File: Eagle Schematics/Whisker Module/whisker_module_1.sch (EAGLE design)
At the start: 135 parts, among them IC1 74LS14N, IC2 74LS14N, IC3 74LS14N, IC4 74LS14N, IC5 74LS14N, IC6 74LS14N, IC7 74LS14N, M1 CD74HCT151E, M2 CD74HCT151E, M3 CD74HCT151E, M4 CD74HCT151E, M5 CD74HCT151E, X1 22-23-2021, X10 22-23-2021, X11 22-23-2021, X12 22-23-2021, X13 22-23-2021, X14 22-23-2021, X15 22-23-2021, X16 22-23-2021, X17 22-23-2021, X18 22-23-2021, X19 22-23-2021, X2 22-23-2021, X20 22-23-2021, X21 22-23-2021, X22 22-23-2021, X23 22-23-2021, X24 22-23-2021, X25 22-23-2021, X26 22-23-2021, X27 22-23-2021, X28 22-23-2021, X29 22-23-2021, X3 22-23-2021, X30 22-23-2021, X31 22-23-2021, X32 22-23-2021, X33 22-23-2021, X34 22-23-2021, X35 22-23-2021, X36 22-23-2021, X37 22-23-2021, X38 22-23-2021, X39 22-23-2021, X4 22-23-2021, X40 22-23-2021, X5 22-23-2021, X6 22-23-2021, X7 22-23-2021, X8 22-23-2021, X9 22-23-2021

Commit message: Finished V1.0 whisker module
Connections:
- removed net N$2: X1-1.S, X10-1.S, X11-1.S, X12-1.S, X13-1.S, X14-1.S, X15-1.S, X16-1.S, X17-1.S, X18-1.S, X19-1.S, X2-1.S, X20-1.S, X21-1.S, X22-1.S, X23-1.S, X24-1.S, X25-1.S, X26-1.S, X27-1.S, X28-1.S, X29-1.S, X3-1.S, X30-1.S, X31-1.S, X32-1.S, X33-1.S, X34-1.S, X35-1.S, X36-1.S, X37-1.S, X38-1.S, X39-1.S, X4-1.S, X40-1.S, X5-1.S, X6-1.S, X7-1.S, X8-1.S, X9-1.S
- net GND: now also X1-1.S, X10-1.S, X11-1.S, X12-1.S, X13-1.S, X14-1.S, X15-1.S, X16-1.S, X17-1.S, X18-1.S, X19-1.S, X2-1.S, X20-1.S, X21-1.S, X22-1.S, X23-1.S, X24-1.S, X25-1.S, X26-1.S, X27-1.S, X28-1.S, X29-1.S, X3-1.S, X30-1.S, X31-1.S, X32-1.S, X33-1.S, X34-1.S, X35-1.S, X36-1.S, X37-1.S, X38-1.S, X39-1.S, X4-1.S, X40-1.S, X5-1.S, X6-1.S, X7-1.S, X8-1.S, X9-1.S

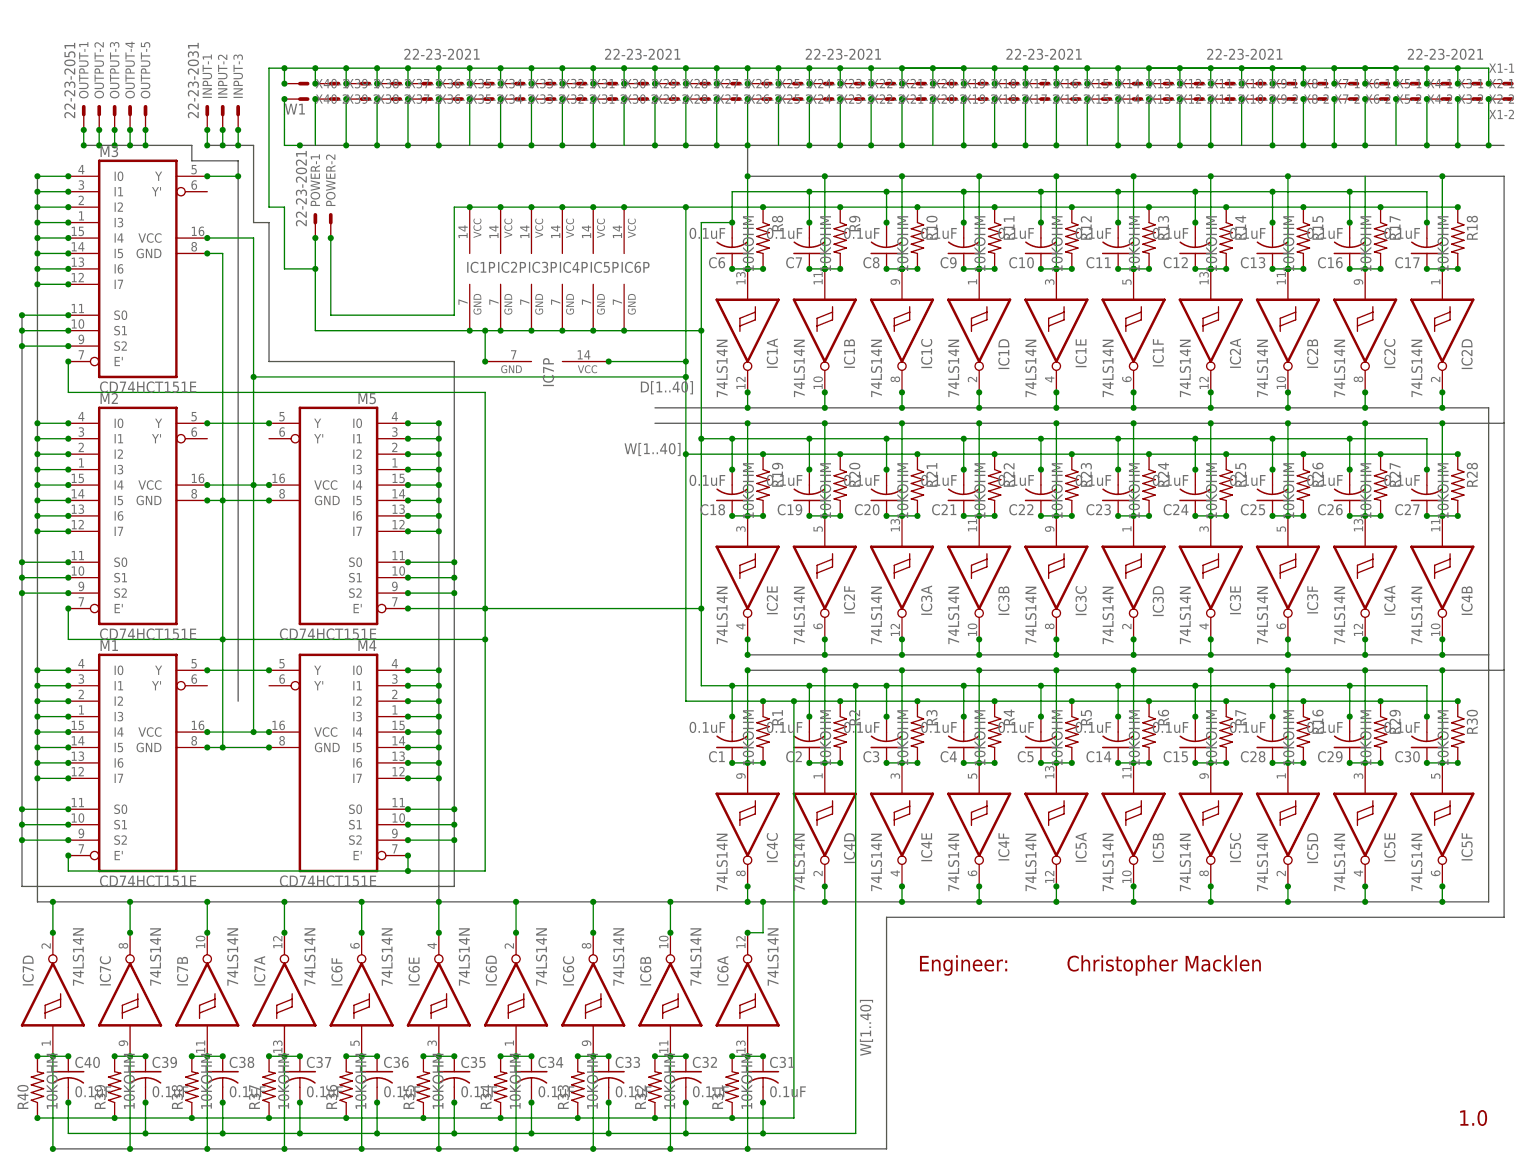
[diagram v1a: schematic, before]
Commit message: Finished both whisker modules
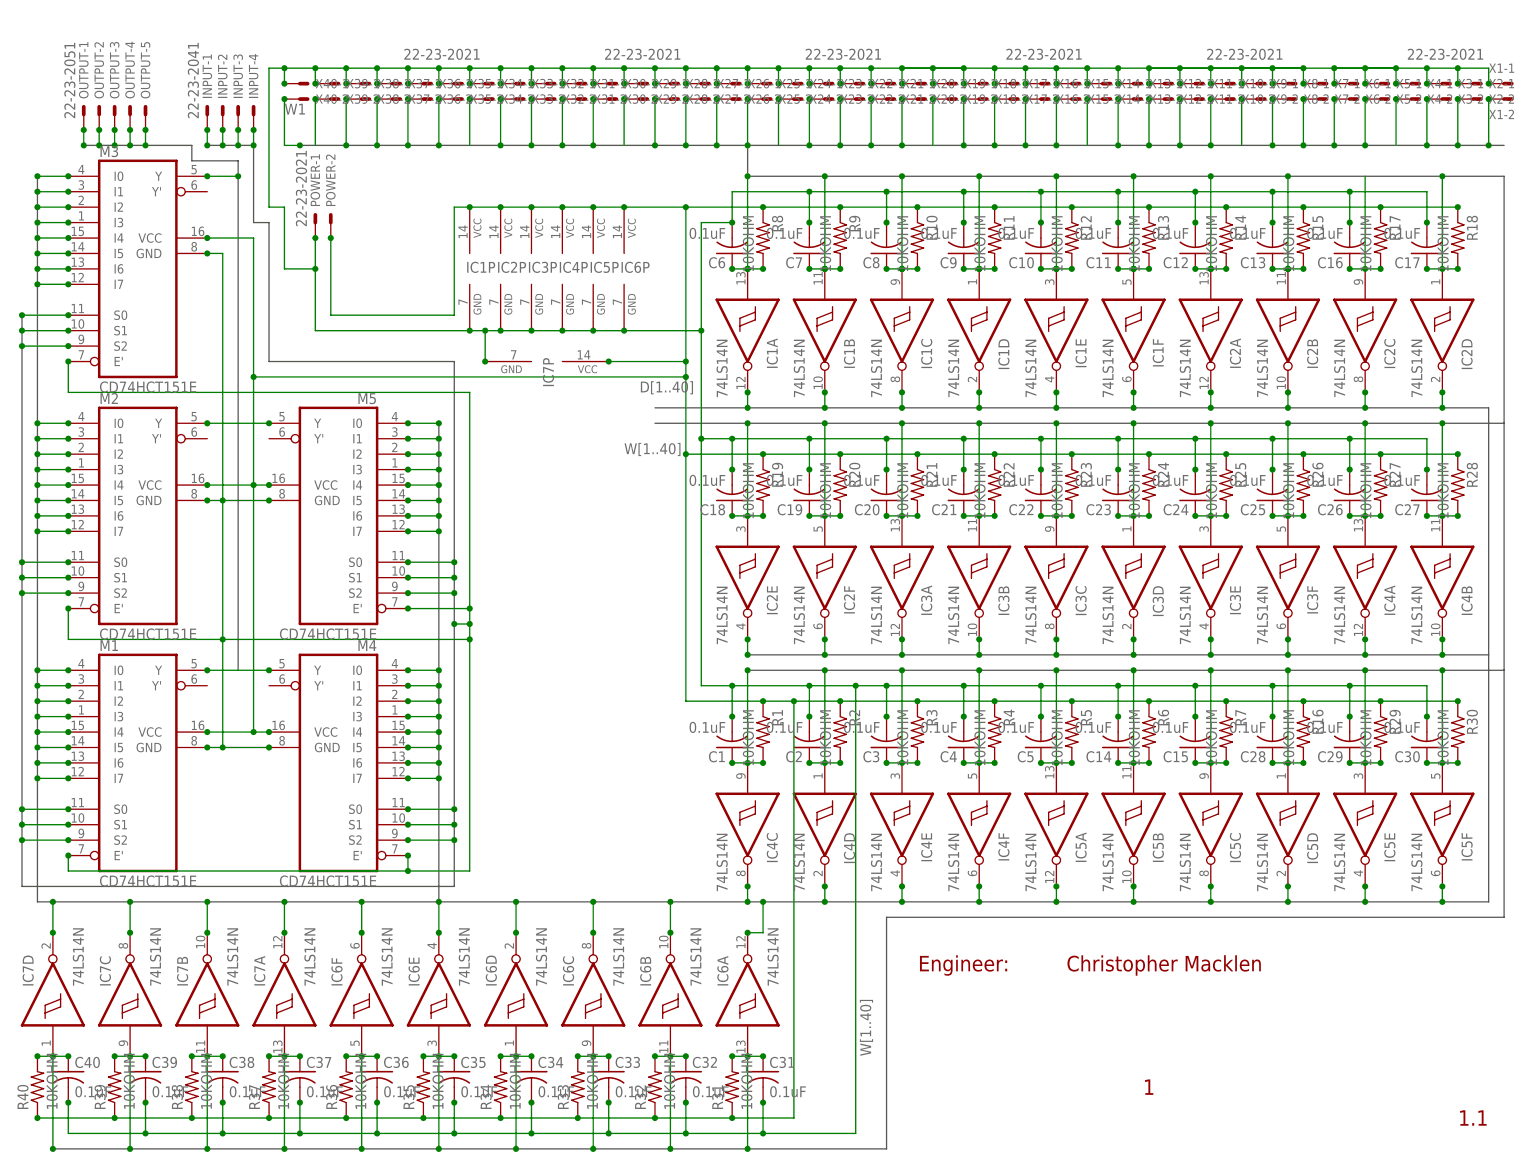
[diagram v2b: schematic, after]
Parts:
- INPUT: value 22-23-2031 -> 22-23-2041; device con-molex:22-23-2031 -> con-molex:22-23-2041
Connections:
- new net SELECT4: INPUT-4.S, M1.E', M1.GND, M2.E', M2.GND, M3.E', M3.GND, M4.E', M4.GND, M5.E', M5.GND
- net GND: no longer M1.E', M1.GND, M2.E', M2.GND, M3.E', M3.GND, M4.E', M4.GND, M5.E', M5.GND
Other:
- note added: "1"
- note added: "1.1"
- note removed: "1.0"
